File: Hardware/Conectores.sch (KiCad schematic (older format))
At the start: 16 parts, among them J101 ENGINE_VEL, J102 ENGINE_ACEL, J103 MPPT_POT, J104 SW_PUMP1_ON, J105 SW_PUMP2_ON, J106 SW_PUMP3_ON, J107 SW_BOAT_ON, J108 SW_ENGINE_ON, J109 SW_MPPT_ON, J110 SW_DMS, J111 SW_EMERGENCIA

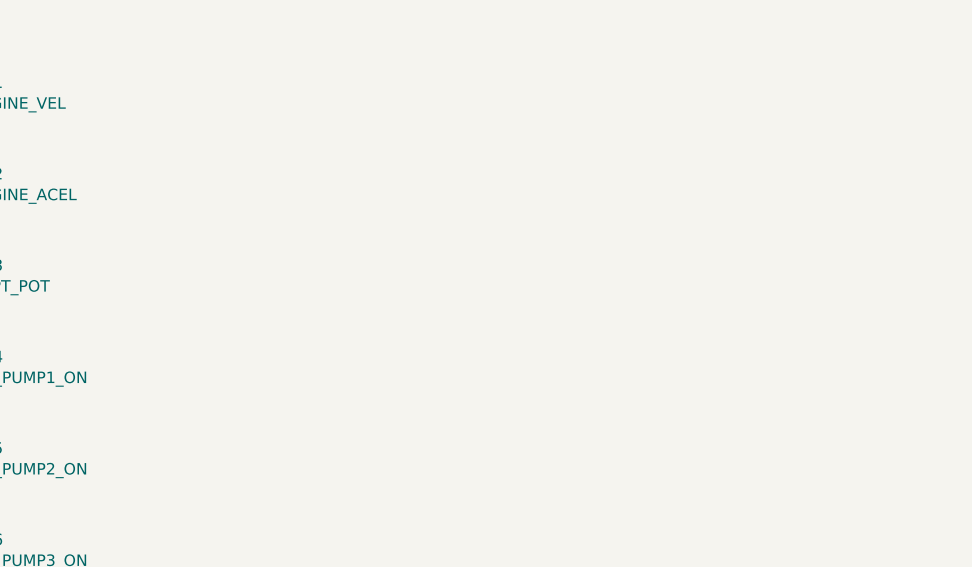
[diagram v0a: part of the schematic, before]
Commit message: Formato da placa modificado
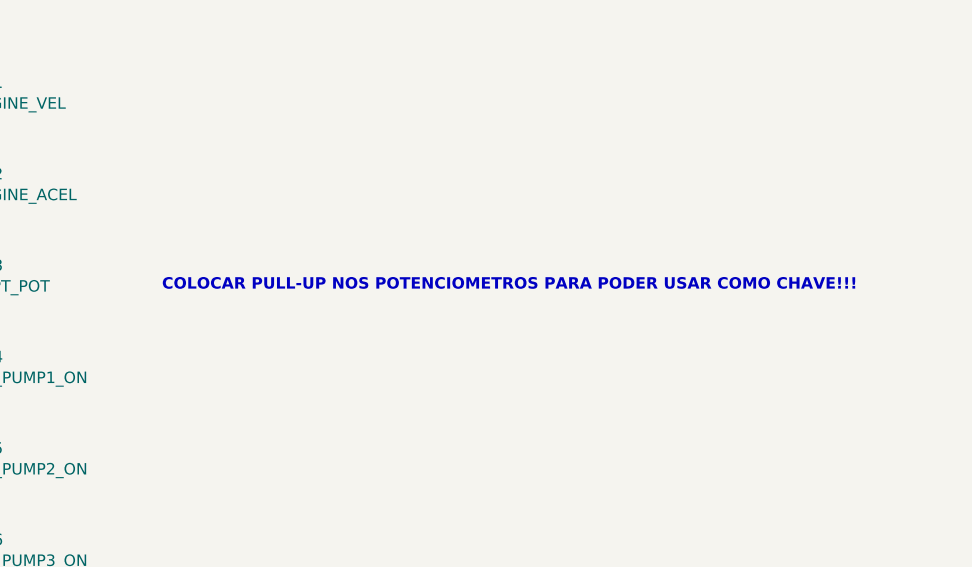
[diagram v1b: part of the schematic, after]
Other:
- note added: "COLOCAR PULL-UP NOS POTENCIOMETROS PARA PODER USAR COMO CHAVE!!!"
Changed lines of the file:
@@
 EESchema Schematic File Version 4
 LIBS:MIC19-cache
-EELAYER 26 0
+EELAYER 29 0
 EELAYER END
 $Descr A4 11693 8268
 encoding utf-8
-Sheet 6 6
+Sheet 5 6
 Title ""
 Date ""
@@
 Wire Wire Line
 	5675 1575 4425 1575
+Text Notes 6800 2450 0    50   ~ 10
+COLOCAR PULL-UP NOS POTENCIOMETROS PARA PODER USAR COMO CHAVE!!!
 $EndSCHEMATC

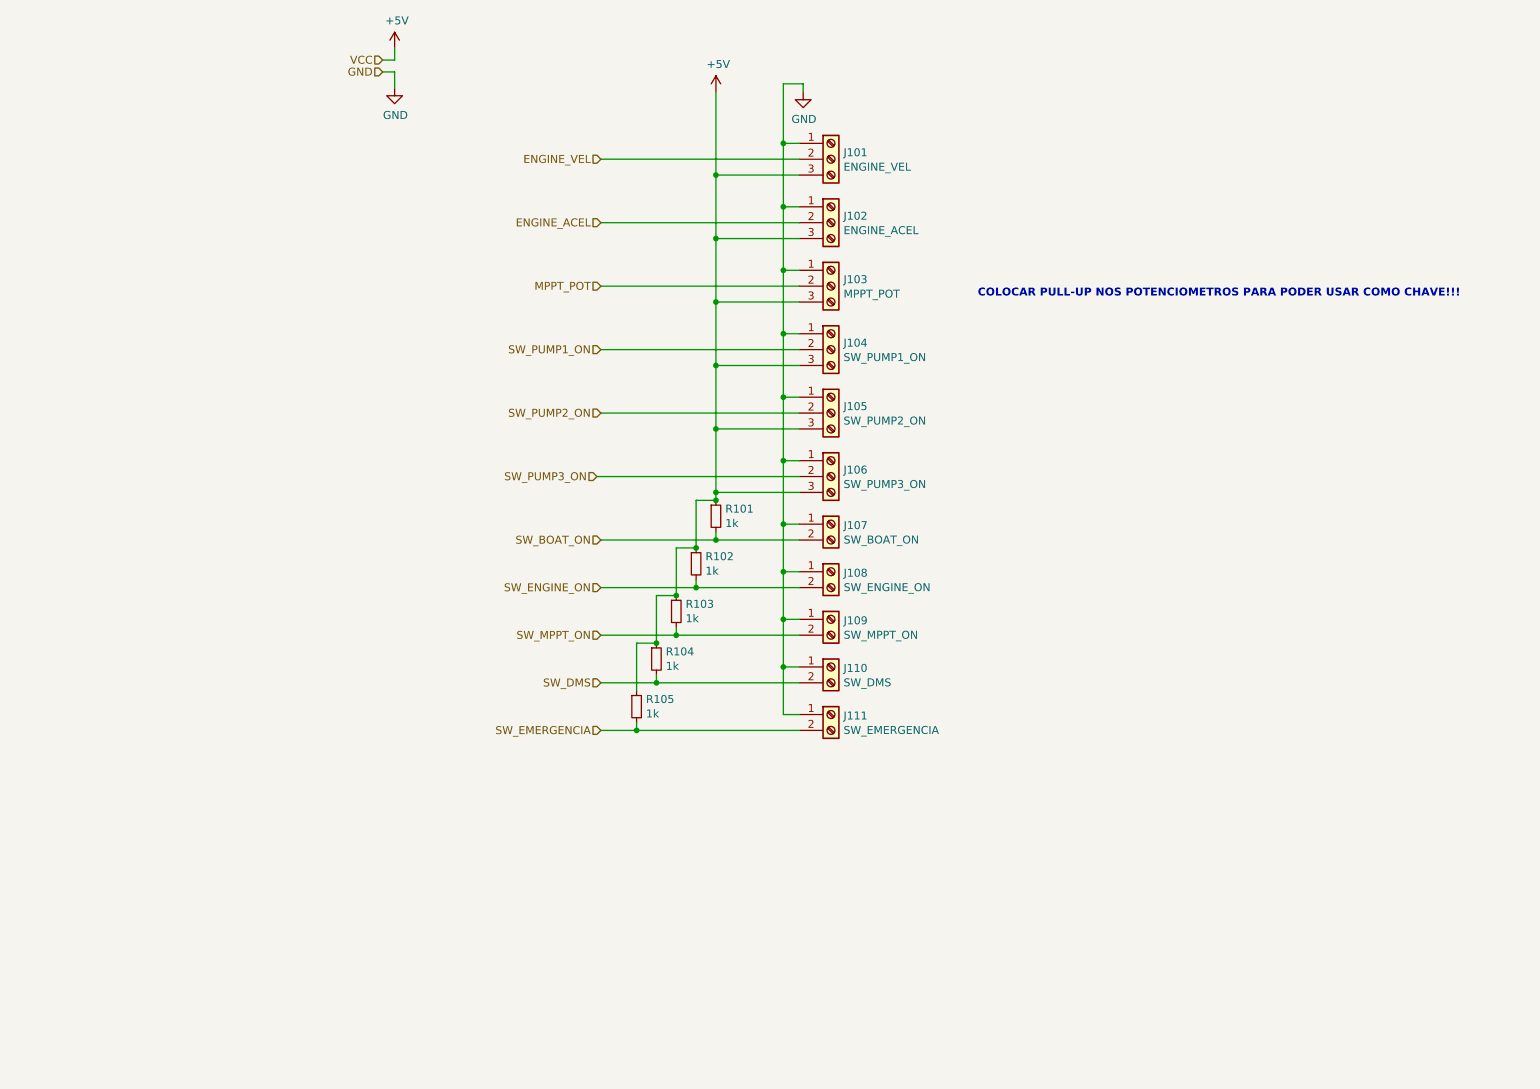
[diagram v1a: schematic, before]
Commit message: Modificaçoes nos resistores pull-up e modificaçoes no layout
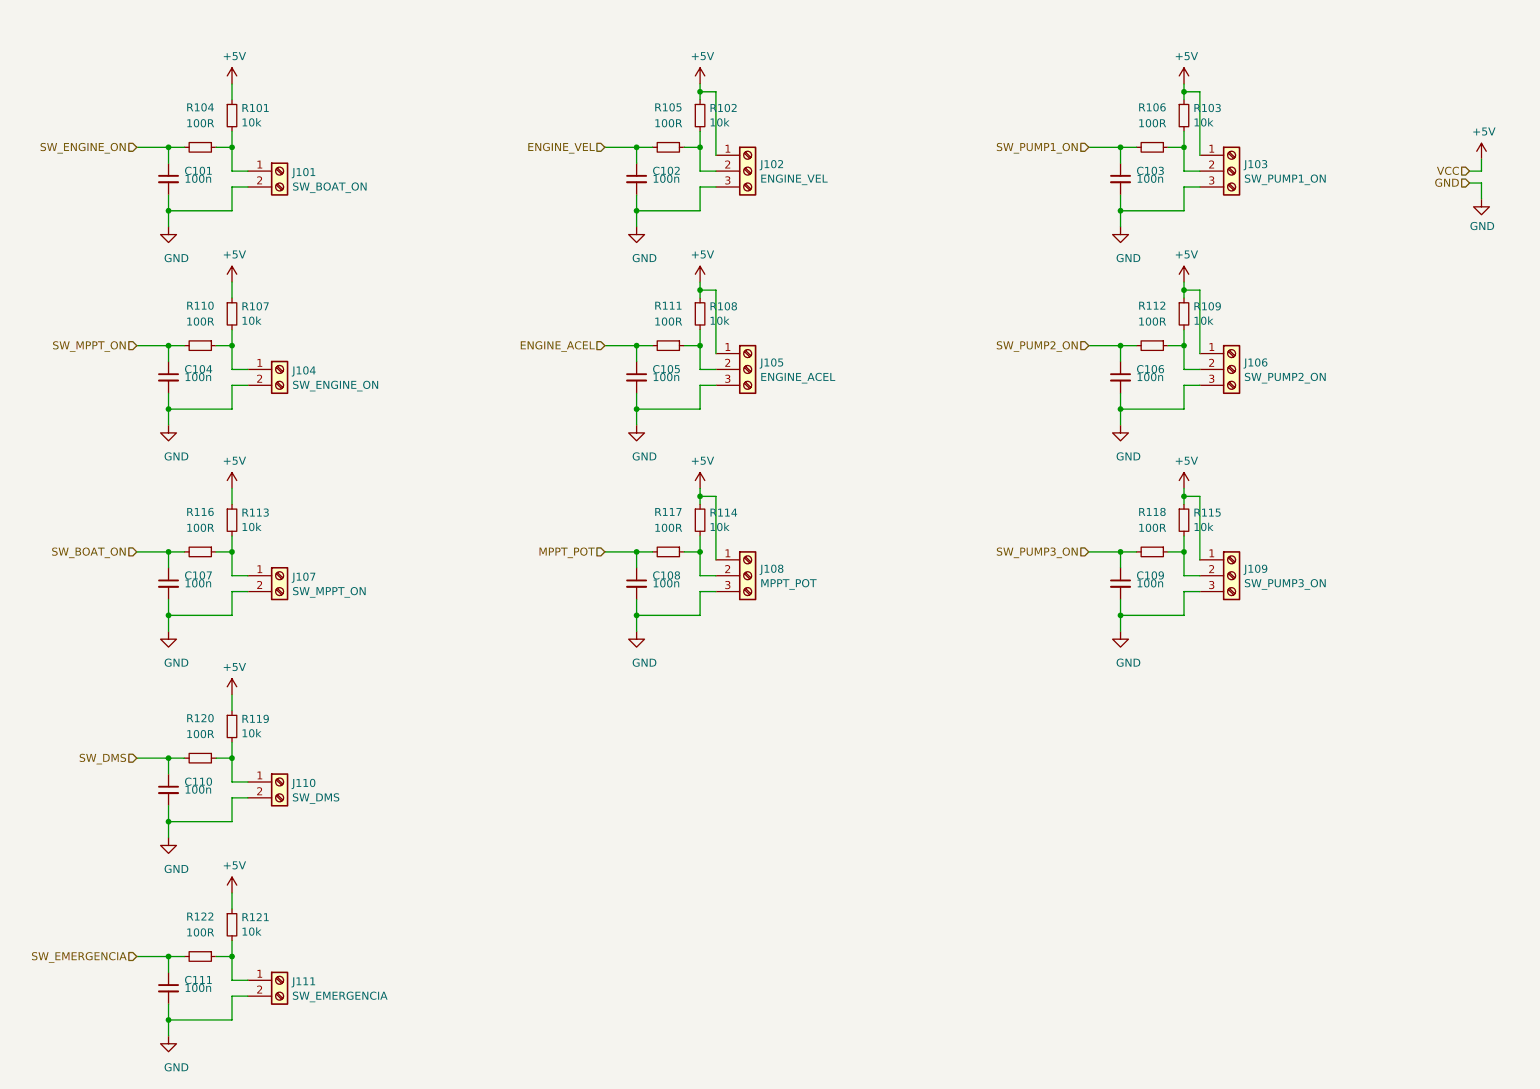
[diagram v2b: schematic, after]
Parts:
- added C101, C102, C103, C104, C105, C106, C107, C108, C109, C110, C111: 100n, Capacitor_SMD:C_0805_2012Metric_Pad1.15x1.40mm_HandSolder, symbol Device:C_Small
- added R106, R110, R111, R112, R116, R117, R118, R120, R122: 100R, Resistor_SMD:R_0805_2012Metric_Pad1.15x1.40mm_HandSolder, symbol Device:R_Small
- added R107, R108, R109, R113, R114, R115, R119, R121: 10k, Resistor_SMD:R_0805_2012Metric_Pad1.15x1.40mm_HandSolder, symbol Device:R_Small
- R101, R102, R103: value 1k -> 10k
- R104, R105: value 1k -> 100R
- renumbered J107 to J101, J101 to J102, J104 to J103, J108 to J104, J102 to J105, J105 to J106, J109 to J107, J103 to J108, J106 to J109
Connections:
- net +5V: now also J102.1 (Pin_1), J103.1 (Pin_1), J105.1 (Pin_1), J106.1 (Pin_1), J108.1 (Pin_1), J109.1 (Pin_1), R107.1, R108.1, R109.1, R113.1, R114.1, R115.1, R119.1, R121.1; no longer J102.3 (Pin_3), J103.3 (Pin_3), J105.3 (Pin_3), J106.3 (Pin_3), J108.3 (Pin_3), J109.3 (Pin_3), R104.1, R105.1
- net ENGINE_ACEL: now also C105.1, R111.2; no longer J105.2 (Pin_2)
- net ENGINE_VEL: now also R105.2, C102.1; no longer J102.2 (Pin_2)
- net GND: now also J101.2 (Pin_2), J102.3 (Pin_3), J103.3 (Pin_3), J104.2 (Pin_2), J105.3 (Pin_3), J106.3 (Pin_3), J107.2 (Pin_2), J108.3 (Pin_3), J109.3 (Pin_3), J110.2 (Pin_2), J111.2 (Pin_2), C101.2, C102.2, C103.2, C104.2, C105.2, C106.2, C107.2, C108.2, C109.2, C110.2, C111.2; no longer J101.1 (Pin_1), J102.1 (Pin_1), J103.1 (Pin_1), J104.1 (Pin_1), J105.1 (Pin_1), J106.1 (Pin_1), J107.1 (Pin_1), J108.1 (Pin_1), J109.1 (Pin_1), J110.1 (Pin_1), J111.1 (Pin_1)
- net MPPT_POT: now also C108.1, R117.2; no longer J108.2 (Pin_2)
- net SW_BOAT_ON: now also C107.1, R116.2; no longer J101.2 (Pin_2), R101.2
- net SW_DMS: now also C110.1, R120.2; no longer J110.2 (Pin_2), R104.2
- net SW_EMERGENCIA: now also C111.1, R122.2; no longer J111.2 (Pin_2), R105.2
- net SW_ENGINE_ON: now also R104.2, C101.1; no longer J104.2 (Pin_2), R102.2
- net SW_MPPT_ON: now also C104.1, R110.2; no longer J107.2 (Pin_2), R103.2
- net SW_PUMP1_ON: now also C103.1, R106.2; no longer J103.2 (Pin_2)
- net SW_PUMP2_ON: now also C106.1, R112.2; no longer J106.2 (Pin_2)
- net SW_PUMP3_ON: now also C109.1, R118.2; no longer J109.2 (Pin_2)
- new net: J108.2 (Pin_2), R114.2, R117.1
- new net: J105.2 (Pin_2), R108.2, R111.1
- new net: J102.2 (Pin_2), R102.2, R105.1
- new net: J101.1 (Pin_1), R101.2, R104.1
- new net: J104.1 (Pin_1), R107.2, R110.1
- new net: J107.1 (Pin_1), R113.2, R116.1
- new net: J110.1 (Pin_1), R119.2, R120.1
- new net: J103.2 (Pin_2), R103.2, R106.1
- new net: J106.2 (Pin_2), R109.2, R112.1
- new net: J109.2 (Pin_2), R115.2, R118.1
- new net: J111.1 (Pin_1), R121.2, R122.1
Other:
- note removed: "COLOCAR PULL-UP NOS POTENCIOMETROS PARA PODER USAR COMO CHAVE!!!"
- moved on the sheet: J101, J102, J103, J104, J105, J106, J107, J108, J109, J110, J111, R101
